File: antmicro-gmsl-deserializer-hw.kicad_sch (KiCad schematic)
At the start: 0 parts

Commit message: Schematics done
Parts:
- added H1, H2, H3, H4: Spacer_Drill3.7mm_H2.5mm_9774025151R, antmicro-footprints:Spacer_Drill3.7mm_H2.5mm_9774025151R, symbol antmicroMechanicalParts:Spacer_Drill3.7mm_H2.5mm_9774025151R
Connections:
- new net GND: H1.1, H2.1, H3.1, H4.1

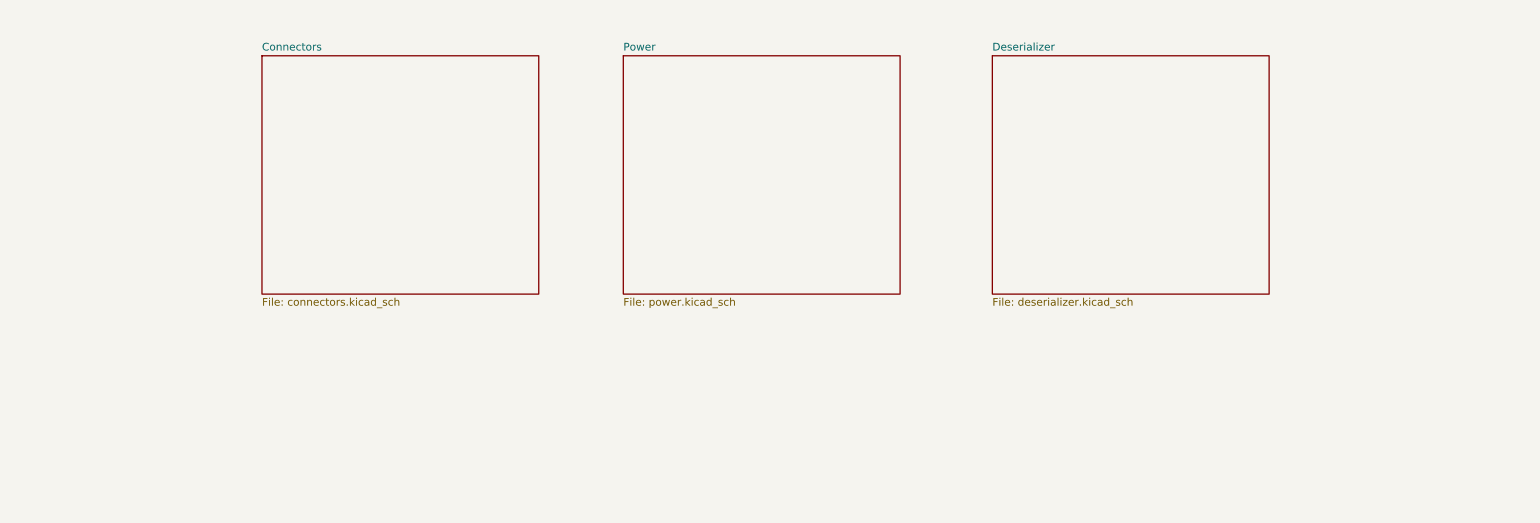
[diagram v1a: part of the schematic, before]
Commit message: Schematics: Fix buses, change labels to hierarchical
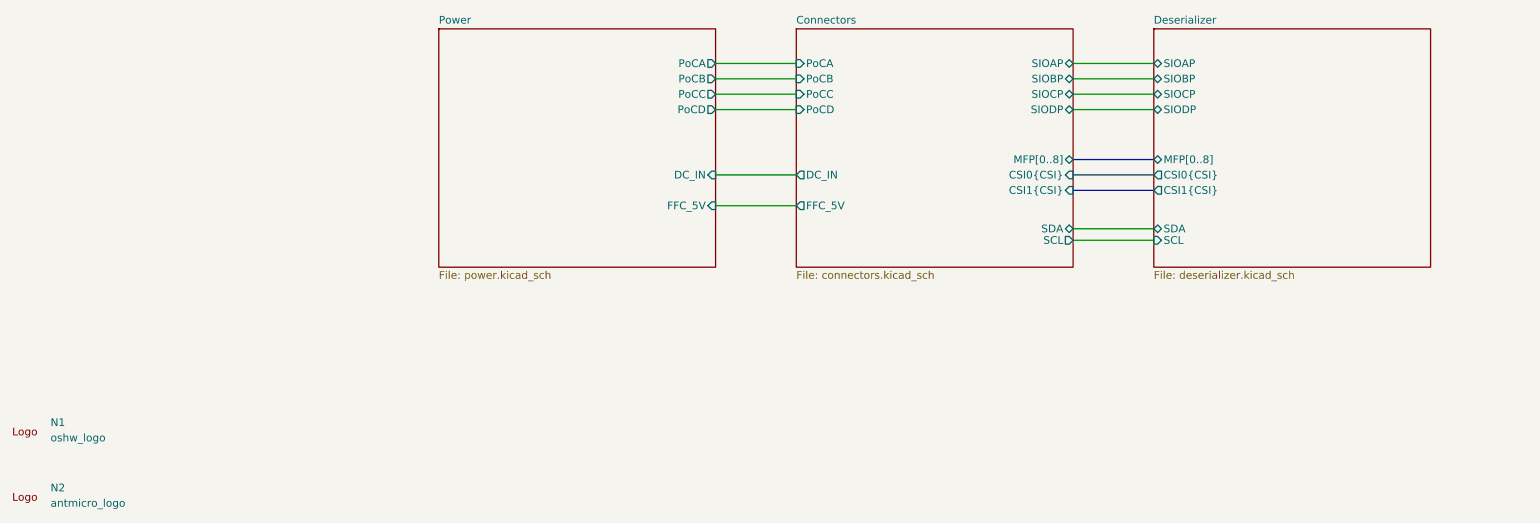
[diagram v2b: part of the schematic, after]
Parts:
- added N1: oshw_logo, antmicro-footprints:oshw-logo, symbol antmicroMechanicalParts:oshw_logo
- added N2: antmicro_logo, antmicro-footprints:antmicro-logo_scaled_12mm, symbol antmicroMechanicalParts:antmicro_logo
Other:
- sheet Connectors ports: added CSI0{CSI}, CSI1{CSI}, DC_IN, FFC_5V, MFP[0..8], PoCA, PoCB, PoCC, PoCD, SCL, SDA, SIOAP, SIOBP, SIOCP, SIODP; removed none
- sheet Deserializer ports: added CSI0{CSI}, CSI1{CSI}, MFP[0..8], SCL, SDA, SIOAP, SIOBP, SIOCP, SIODP; removed none
- sheet Power ports: added DC_IN, FFC_5V, PoCA, PoCB, PoCC, PoCD; removed none
